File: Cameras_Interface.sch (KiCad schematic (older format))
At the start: 18 parts, among them J9 WE_68715014522, U9 MAX13042EEBC+T

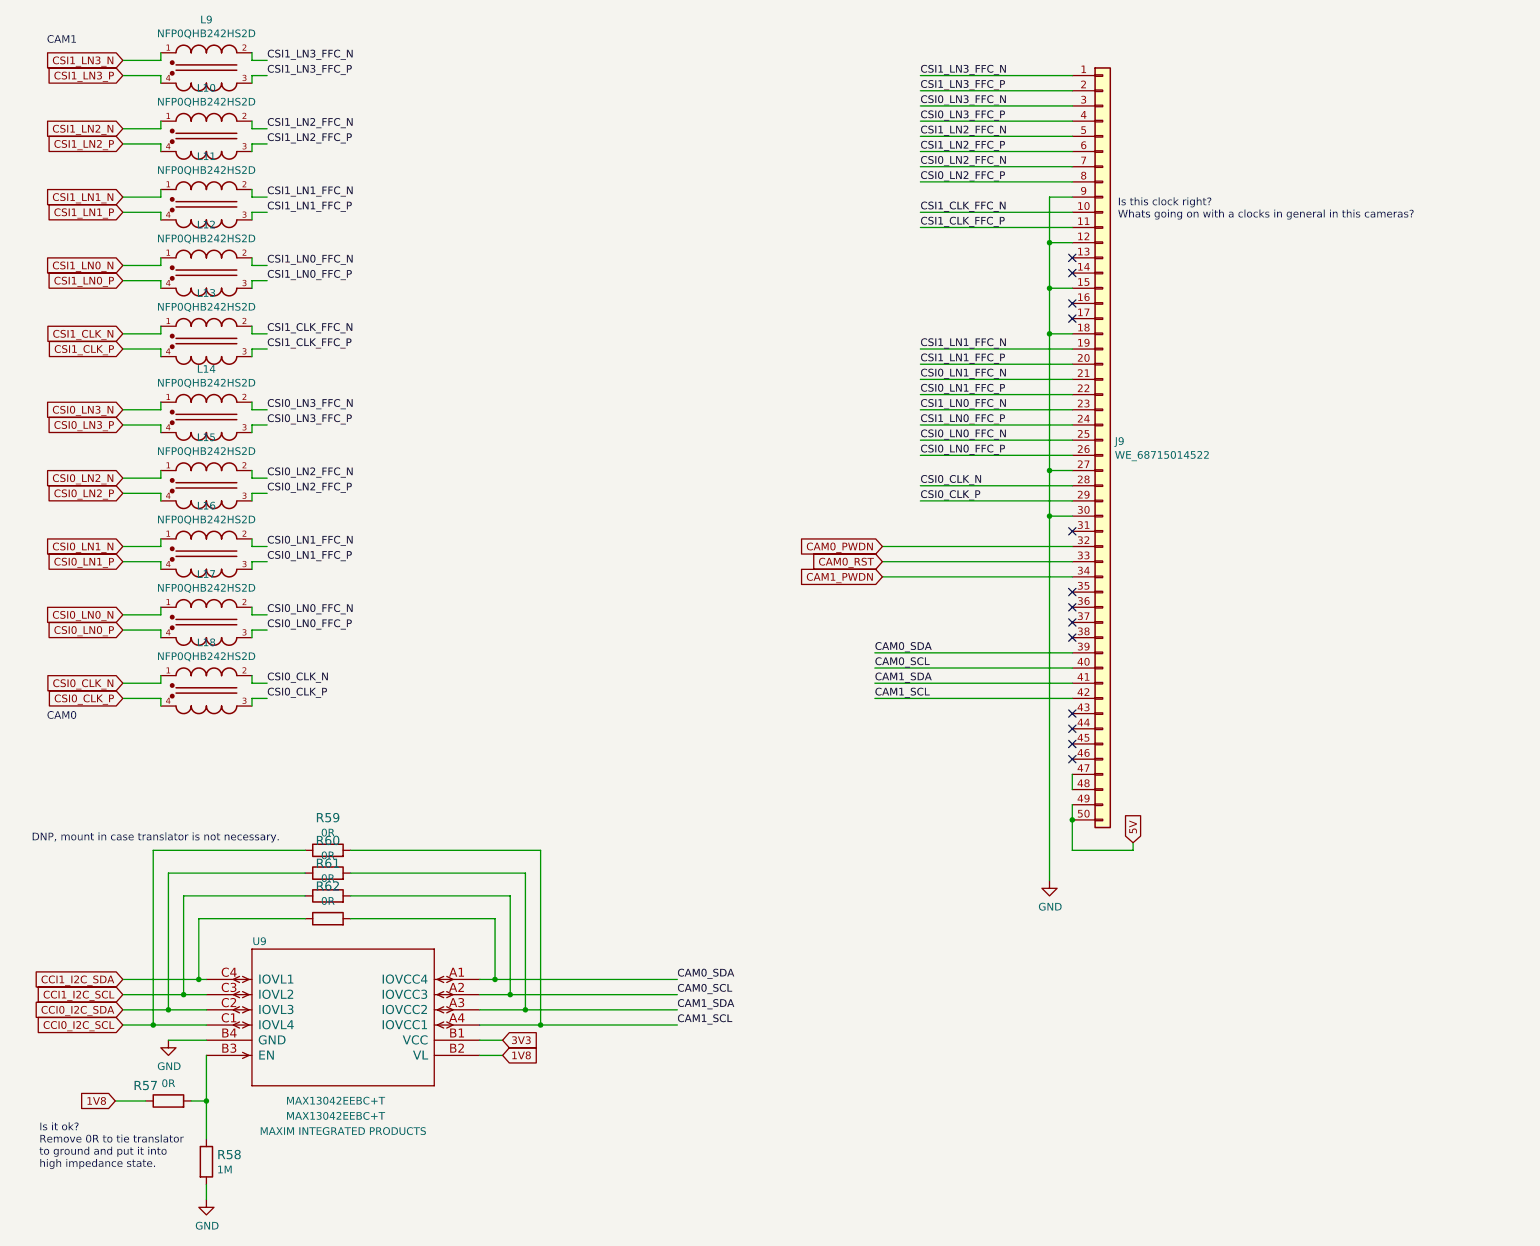
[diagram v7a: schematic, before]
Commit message: cleaned up components fields
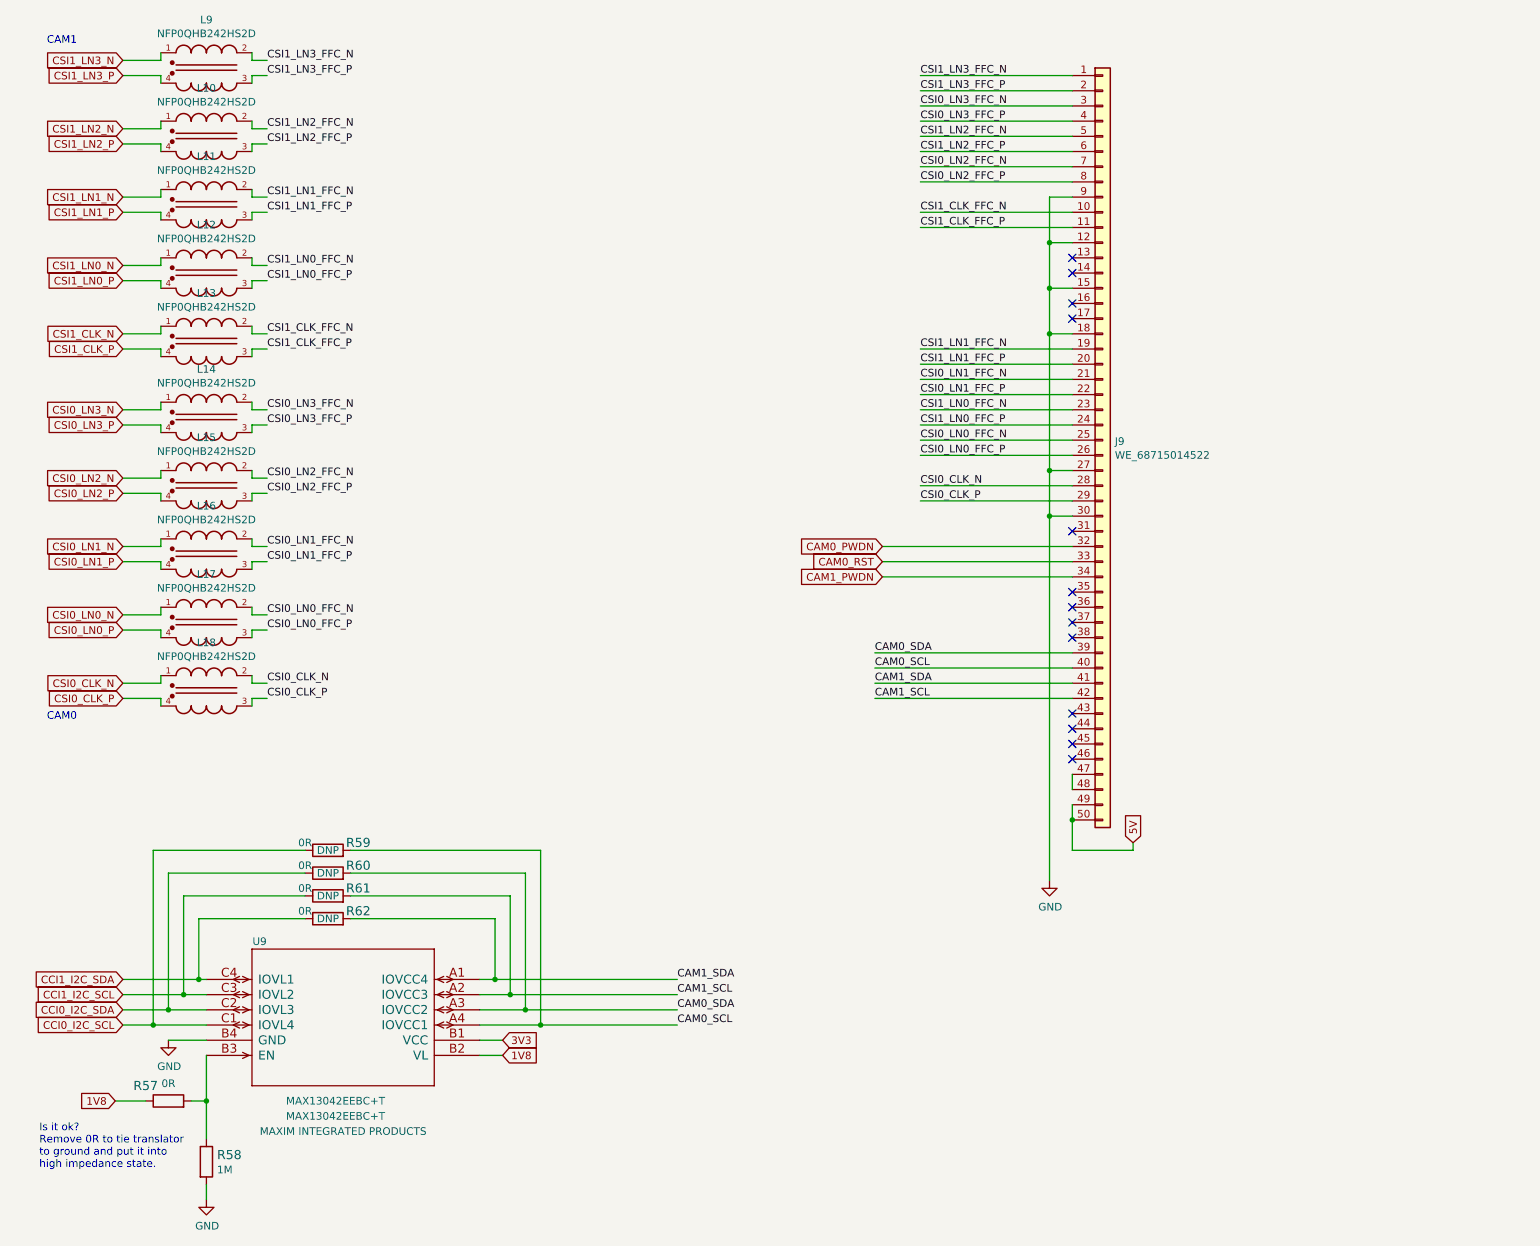
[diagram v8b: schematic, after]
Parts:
- R61: DNP (none) -> DNP; Field7 DNP -> (none)
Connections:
- net CAM0_SCL: now also R59.2, U9.A4 (IOVCC1); no longer R61.2, U9.A2 (IOVCC3)
- net CAM0_SDA: now also R60.2, U9.A3 (IOVCC2); no longer R62.2, U9.A1 (IOVCC4)
- net CAM1_SCL: now also R61.2, U9.A2 (IOVCC3); no longer R59.2, U9.A4 (IOVCC1)
- net CAM1_SDA: now also R62.2, U9.A1 (IOVCC4); no longer R60.2, U9.A3 (IOVCC2)
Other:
- note removed: "DNP, mount in case translator is not necessary."
- note removed: "Is this clock right?\nWhats going on with a clocks in general in this cameras?\n"
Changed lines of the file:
@@
 $Descr A3 16535 11693
 encoding utf-8
-Sheet 8 11
+Sheet 7 11
 Title ""
 Date ""
@@
 Wire Wire Line
 	6450 2650 7450 2650
-Text Notes 7750 2600 0    50   ~ 0
-Is this clock right?\nWhats going on with a clocks in general in this cameras?\n
 Wire Wire Line
 	7450 2750 7300 2750
@@
 Text GLabel 1200 7700 0    50   Input ~ 0
 CCI1_I2C_SCL
+Text Label 4850 7800 0    50   ~ 0
+CAM0_SDA
+Text Label 4850 7900 0    50   ~ 0
+CAM0_SCL
 Text Label 4850 7600 0    50   ~ 0
-CAM0_SDA
+CAM1_SDA
 Text Label 4850 7700 0    50   ~ 0
-CAM0_SCL
-Text Label 4850 7800 0    50   ~ 0
-CAM1_SDA
-Text Label 4850 7900 0    50   ~ 0
 CAM1_SCL
 Wire Wire Line
@@
 U 1 1 61CF2C26
 P 2550 6750
-F 0 "R59" H 2550 6963 60  0000 C CNN
+F 0 "R59" H 2750 6800 60  0000 C CNN
 F 1 "R_0R_0603" H 2550 6600 60  0001 C CNN
 F 2 "antmicro-footprints:0603-res" H 2750 6950 60  0001 L CNN
@@
 F 4 "BOURNS" H 2750 7150 60  0001 L CNN "Manufacturer"
 F 5 "CR0603-J/-000ELF" H 2750 7050 60  0001 L CNN "MPN"
-F 6 "0R" H 2550 6865 50  0000 C CNN "Val"
-F 7 "DNP" H 2550 6750 50  0001 C CNN "DNP"
+F 6 "0R" H 2400 6800 50  0000 C CNN "Val"
+F 7 "DNP" H 2550 6750 50  0000 C CNN "DNP"
 	1    2550 6750
 	1    0    0    -1
@@
 U 1 1 61CF310B
 P 2550 6900
-F 0 "R60" H 2550 7113 60  0000 C CNN
+F 0 "R60" H 2750 6950 60  0000 C CNN
 F 1 "R_0R_0603" H 2550 6750 60  0001 C CNN
 F 2 "antmicro-footprints:0603-res" H 2750 7100 60  0001 L CNN
@@
 F 4 "BOURNS" H 2750 7300 60  0001 L CNN "Manufacturer"
 F 5 "CR0603-J/-000ELF" H 2750 7200 60  0001 L CNN "MPN"
-F 6 "0R" H 2550 7015 50  0000 C CNN "Val"
-F 7 "DNP" H 2550 6900 50  0001 C CNN "DNP"
+F 6 "0R" H 2400 6950 50  0000 C CNN "Val"
+F 7 "DNP" H 2550 6900 50  0000 C CNN "DNP"
 	1    2550 6900
 	1    0    0    -1
@@
 U 1 1 61CF351C
 P 2550 7050
-F 0 "R61" H 2550 7263 60  0000 C CNN
+F 0 "R61" H 2750 7100 60  0000 C CNN
 F 1 "R_0R_0603" H 2550 6900 60  0001 C CNN
 F 2 "antmicro-footprints:0603-res" H 2750 7250 60  0001 L CNN
@@
 F 4 "BOURNS" H 2750 7450 60  0001 L CNN "Manufacturer"
 F 5 "CR0603-J/-000ELF" H 2750 7350 60  0001 L CNN "MPN"
-F 6 "0R" H 2550 7165 50  0000 C CNN "Val"
-F 7 "DNP" H 2550 7050 50  0001 C CNN "Field7"
+F 6 "0R" H 2400 7100 50  0000 C CNN "Val"
+F 7 "DNP" H 2550 7050 50  0000 C CNN "DNP"
 	1    2550 7050
 	1    0    0    -1
@@
 U 1 1 61CF37C7
 P 2550 7200
-F 0 "R62" H 2550 7413 60  0000 C CNN
+F 0 "R62" H 2750 7250 60  0000 C CNN
 F 1 "R_0R_0603" H 2550 7050 60  0001 C CNN
 F 2 "antmicro-footprints:0603-res" H 2750 7400 60  0001 L CNN
@@
 F 4 "BOURNS" H 2750 7600 60  0001 L CNN "Manufacturer"
 F 5 "CR0603-J/-000ELF" H 2750 7500 60  0001 L CNN "MPN"
-F 6 "0R" H 2550 7315 50  0000 C CNN "Val"
-F 7 "DNP" H 2550 7200 50  0001 C CNN "DNP"
+F 6 "0R" H 2400 7250 50  0000 C CNN "Val"
+F 7 "DNP" H 2550 7200 50  0000 C CNN "DNP"
 	1    2550 7200
 	1    0    0    -1
@@
 Text Notes 650  8850 0    50   ~ 0
 Is it ok?\nRemove 0R to tie translator \nto ground and put it into\nhigh impedance state.
-Text Notes 600  6700 0    50   ~ 0
-DNP, mount in case translator is not necessary.
 Wire Wire Line
 	7450 6450 7450 6550
